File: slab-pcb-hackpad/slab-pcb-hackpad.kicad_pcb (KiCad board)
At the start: 2 copper layers, 120 x 95 mm, 108 parts, among them J1 MagnetR, J2 MagnetL, J3 TRRS_R, J4 TRRS_L, J5 SSD1306, J6 Conn_01x06, Q1 MMBT3906, U1 Seeeduino Xiao rp2040, U2 PCA9555PW, U3 PCA9555PW, U4 SN74AHCT125PWR

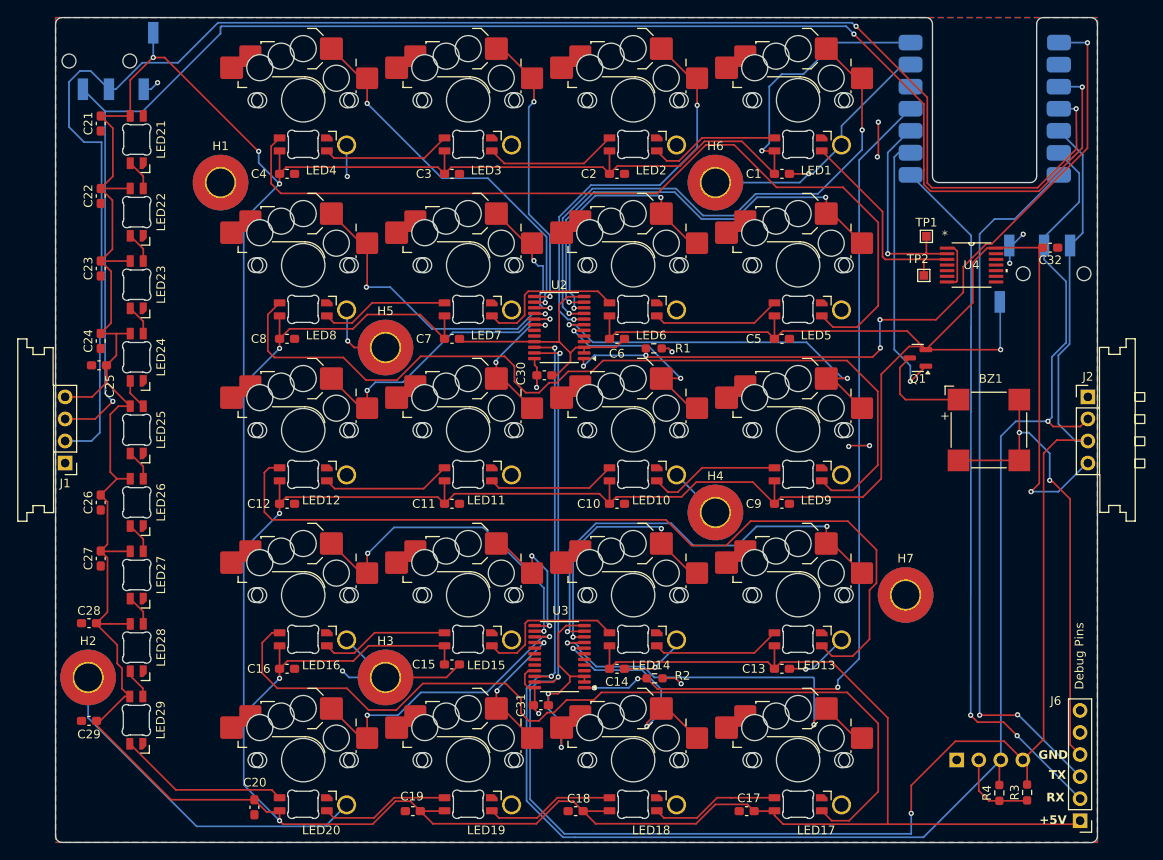
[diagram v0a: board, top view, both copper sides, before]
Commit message: fix: upside-down magnetic connectors
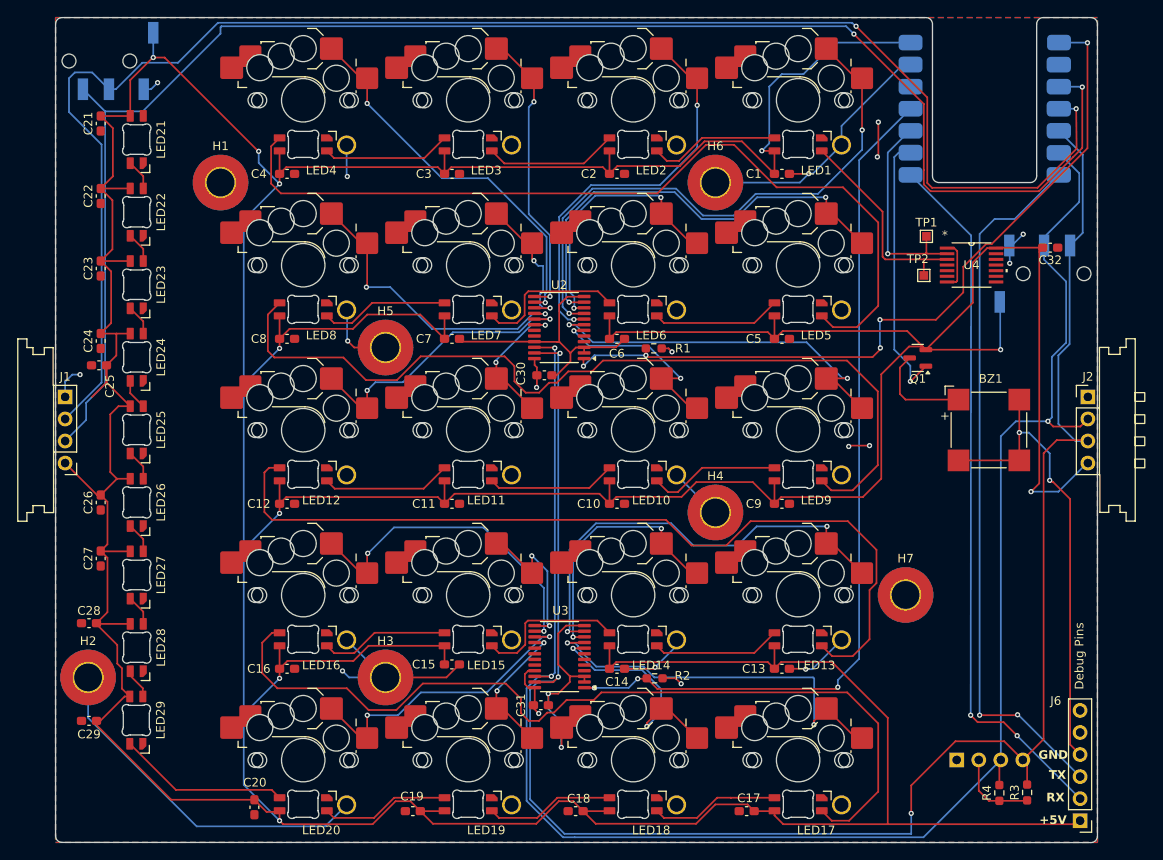
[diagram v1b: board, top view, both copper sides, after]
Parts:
- U4: value SN74AHCT125PWR -> (none)
- turned J1 to 0 degrees
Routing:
- net /I2C0_SCL: track 190.5 -> 185.1 mm
- net GND: track 250.7 -> 254.5 mm, vias 13 -> 14
- net VBUS: track 796.9 -> 799.4 mm
- net /I2C0_SDA: track 185.9 -> 185.6 mm, vias 3 -> 2

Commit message: misc hackpad changes
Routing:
- net VBUS: track 799.4 -> 795.1 mm
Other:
- board text added: "version 3.1 'nowhere'"
- board text removed: "version 3.0 'nowhere'"
